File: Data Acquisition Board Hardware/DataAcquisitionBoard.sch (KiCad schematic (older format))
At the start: 10 parts, among them P1 BNC, P2 BNC, P3 BNC, P4 BNC

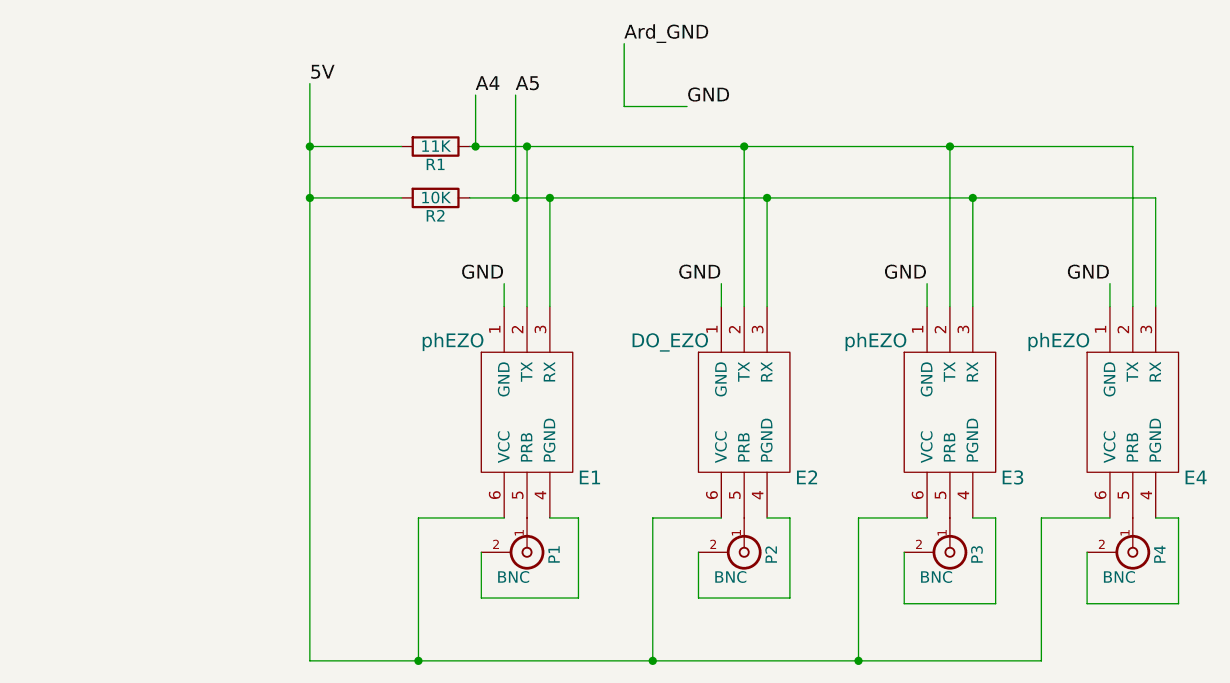
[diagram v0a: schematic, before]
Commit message: Completed PCB layout, added jumper footprint
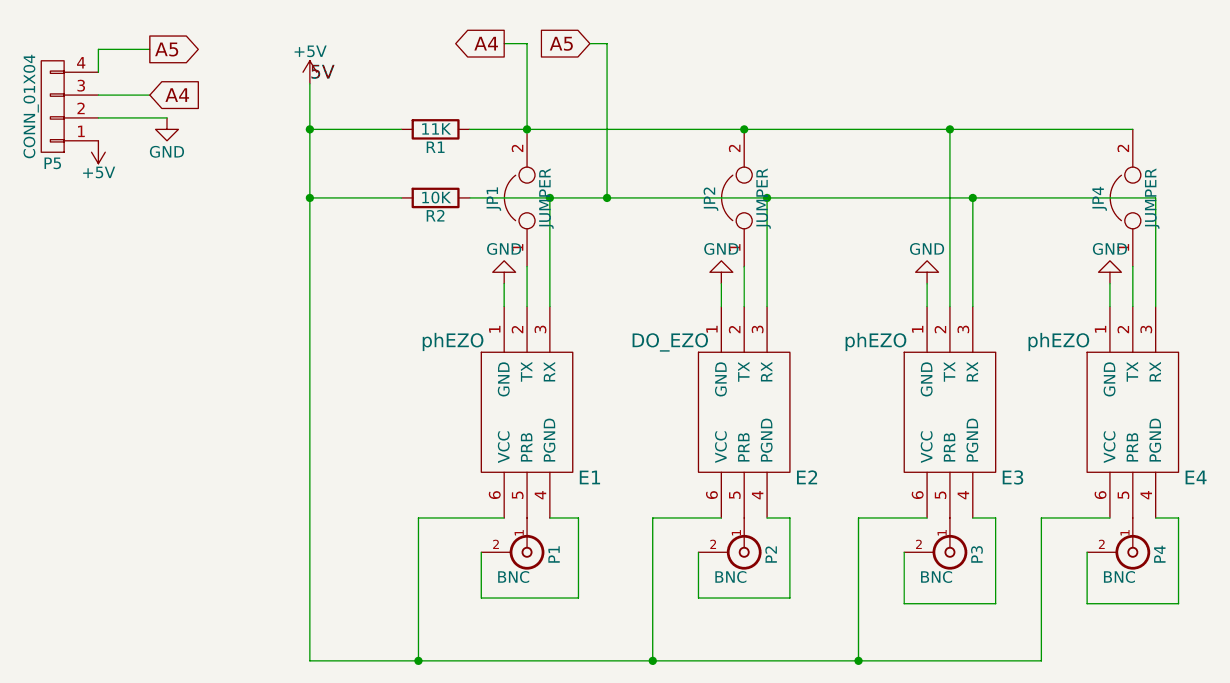
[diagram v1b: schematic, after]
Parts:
- added JP1, JP2, JP4: JUMPER, DAB:Jumper_6.35mm, symbol JUMPER
- added P5: CONN_01X04, Pin_Headers:Pin_Header_Straight_1x04, symbol CONN_01X04
- R1, R2: footprint Resistors_SMD:R_0805_HandSoldering -> Resistors_ThroughHole:Resistor_Horizontal_RM7mm
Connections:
- net A4: now also JP1.2, JP2.2, JP4.2, P5.3 (P3); no longer E1.2 (TX), E2.2 (TX), E4.2 (TX)
- net A5: now also P5.4 (P4)
- net 5V renamed +5V
- net +5V: now also P5.1 (P1)
- net Ard_GND renamed GND
- net GND: now also P5.2 (P2)
- new net: E1.2 (TX), JP1.1
- new net: E2.2 (TX), JP2.1
- new net: E4.2 (TX), JP4.1
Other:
- moved on the sheet: R1
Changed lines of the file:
@@
 	1    0    0    -1
 $EndComp
-Wire Wire Line
-	5375 3125 5500 3125
-Wire Wire Line
-	5500 3125 5500 3475
-Wire Wire Line
-	5500 3475 5075 3475
-Wire Wire Line
-	5075 3475 5075 3275
 $Comp
 L BNC P2
@@
 	0    1    1    0
 $EndComp
-Wire Wire Line
-	6325 3125 6425 3125
-Wire Wire Line
-	6425 3125 6425 3475
-Wire Wire Line
-	6425 3475 6025 3475
-Wire Wire Line
-	6025 3475 6025 3275
 Text Label 4325 1225 0    60   ~ 0
 5V
-Wire Wire Line
-	4325 1225 4325 3750
-Wire Wire Line
-	4325 3750 7525 3750
-Wire Wire Line
-	5825 3750 5825 3125
-Wire Wire Line
-	5825 3125 6125 3125
-Wire Wire Line
-	4800 3750 4800 3125
-Wire Wire Line
-	4800 3125 5175 3125
-Connection ~ 4800 3750
 $Comp
 L phEZO E3
@@
 	0    1    1    0
 $EndComp
-Wire Wire Line
-	6925 3275 6925 3500
-Wire Wire Line
-	6925 3500 7325 3500
-Wire Wire Line
-	7325 3500 7325 3125
-Wire Wire Line
-	7325 3125 7225 3125
-Wire Wire Line
-	7725 3275 7725 3500
-Wire Wire Line
-	7725 3500 8125 3500
-Wire Wire Line
-	8125 3500 8125 3125
-Wire Wire Line
-	8125 3125 8025 3125
-Wire Wire Line
-	6725 3750 6725 3125
-Wire Wire Line
-	6725 3125 7025 3125
-Connection ~ 5825 3750
-Wire Wire Line
-	7525 3750 7525 3125
-Wire Wire Line
-	7525 3125 7825 3125
-Connection ~ 6725 3750
-Wire Wire Line
-	7825 2200 7825 2100
-Text Label 7825 2100 2    60   ~ 0
-GND
-Text Label 5975 1325 0    60   ~ 0
-GND
-Wire Wire Line
-	7025 2200 7025 2100
-Text Label 7025 2100 2    60   ~ 0
-GND
-Wire Wire Line
-	6125 2200 6125 2100
-Text Label 6125 2100 2    60   ~ 0
-GND
-Wire Wire Line
-	5175 2200 5175 2100
-Text Label 5175 2100 2    60   ~ 0
-GND
-Text Label 5050 1275 0    60   ~ 0
-A4
 $Comp
 L R R1
 U 1 1 5848F097
-P 4875 1500
-F 0 "R1" V 4955 1500 50  0000 C CNN
-F 1 "11K" V 4875 1500 50  0000 C CNN
-F 2 "Resistors_SMD:R_0805_HandSoldering" V 4805 1500 50  0001 C CNN
-F 3 "" H 4875 1500 50  0000 C CNN
-	1    4875 1500
+P 4875 1425
+F 0 "R1" V 4955 1425 50  0000 C CNN
+F 1 "11K" V 4875 1425 50  0000 C CNN
+F 2 "Resistors_ThroughHole:Resistor_Horizontal_RM7mm" V 4805 1425 50  0001 C CNN
+F 3 "" H 4875 1425 50  0000 C CNN
+	1    4875 1425
 	0    1    1    0
 $EndComp
@@
 F 0 "R2" V 4955 1725 50  0000 C CNN
 F 1 "10K" V 4875 1725 50  0000 C CNN
-F 2 "Resistors_SMD:R_0805_HandSoldering" V 4805 1725 50  0001 C CNN
+F 2 "Resistors_ThroughHole:Resistor_Horizontal_RM7mm" V 4805 1725 50  0001 C CNN
 F 3 "" H 4875 1725 50  0000 C CNN
 	1    4875 1725
 	0    1    1    0
 $EndComp
-Wire Wire Line
-	4325 1500 4725 1500
-Connection ~ 4325 1500
-Wire Wire Line
-	5025 1500 7925 1500
-Wire Wire Line
-	5275 1500 5275 2200
+$Comp
+L CONN_01X04 P5
+U 1 1 5849CBF9
+P 3200 1325
+F 0 "P5" H 3200 1575 50  0000 C CNN
+F 1 "CONN_01X04" V 3300 1325 50  0000 C CNN
+F 2 "Pin_Headers:Pin_Header_Straight_1x04" H 3200 1325 50  0001 C CNN
+F 3 "" H 3200 1325 50  0000 C CNN
+	1    3200 1325
+	-1   0    0    1
+$EndComp
+$Comp
+L +5V #PWR01
+U 1 1 584C80B9
+P 4325 1225
+F 0 "#PWR01" H 4325 1075 50  0001 C CNN
+F 1 "+5V" H 4325 1365 50  0000 C CNN
+F 2 "" H 4325 1225 50  0000 C CNN
+F 3 "" H 4325 1225 50  0000 C CNN
+	1    4325 1225
+	1    0    0    -1
+$EndComp
+$Comp
+L JUMPER JP1
+U 1 1 584C8796
+P 5275 1725
+F 0 "JP1" H 5275 1875 50  0000 C CNN
+F 1 "JUMPER" H 5275 1645 50  0000 C CNN
+F 2 "DAB:Jumper_6.35mm" H 5275 1725 50  0001 C CNN
+F 3 "" H 5275 1725 50  0000 C CNN
+	1    5275 1725
+	0    -1   -1   0
+$EndComp
+$Comp
+L JUMPER JP2
+U 1 1 584C89B3
+P 6225 1725
+F 0 "JP2" H 6225 1875 50  0000 C CNN
+F 1 "JUMPER" H 6225 1645 50  0000 C CNN
+F 2 "DAB:Jumper_6.35mm" H 6225 1725 50  0001 C CNN
+F 3 "" H 6225 1725 50  0000 C CNN
+	1    6225 1725
+	0    -1   -1   0
+$EndComp
+$Comp
+L JUMPER JP4
+U 1 1 584C8A2C
+P 7925 1725
+F 0 "JP4" H 7925 1875 50  0000 C CNN
+F 1 "JUMPER" H 7925 1645 50  0000 C CNN
+F 2 "DAB:Jumper_6.35mm" H 7925 1725 50  0001 C CNN
+F 3 "" H 7925 1725 50  0000 C CNN
+	1    7925 1725
+	0    -1   -1   0
+$EndComp
+Wire Wire Line
+	5375 3125 5500 3125
+Wire Wire Line
+	5500 3125 5500 3475
+Wire Wire Line
+	5500 3475 5075 3475
+Wire Wire Line
+	5075 3475 5075 3275
+Wire Wire Line
+	6325 3125 6425 3125
+Wire Wire Line
+	6425 3125 6425 3475
+Wire Wire Line
+	6425 3475 6025 3475
+Wire Wire Line
+	6025 3475 6025 3275
+Wire Wire Line
+	4325 1225 4325 3750
+Wire Wire Line
+	4325 3750 7525 3750
+Wire Wire Line
+	5825 3750 5825 3125
+Wire Wire Line
+	5825 3125 6125 3125
+Wire Wire Line
+	4800 3750 4800 3125
+Wire Wire Line
+	4800 3125 5175 3125
+Connection ~ 4800 3750
+Wire Wire Line
+	6925 3275 6925 3500
+Wire Wire Line
+	6925 3500 7325 3500
+Wire Wire Line
+	7325 3500 7325 3125
+Wire Wire Line
+	7325 3125 7225 3125
+Wire Wire Line
+	7725 3275 7725 3500
+Wire Wire Line
+	7725 3500 8125 3500
+Wire Wire Line
+	8125 3500 8125 3125
+Wire Wire Line
+	8125 3125 8025 3125
+Wire Wire Line
+	6725 3750 6725 3125
+Wire Wire Line
+	6725 3125 7025 3125
+Connection ~ 5825 3750
+Wire Wire Line
+	7525 3750 7525 3125
+Wire Wire Line
+	7525 3125 7825 3125
+Connection ~ 6725 3750
+Wire Wire Line
+	7825 2200 7825 2100
+Wire Wire Line
+	7025 2200 7025 2100
+Wire Wire Line
+	6125 2200 6125 2100
+Wire Wire Line
+	5175 2200 5175 2100
+Wire Wire Line
+	4325 1425 4725 1425
+Connection ~ 4325 1425
+Wire Wire Line
+	5025 1425 7925 1425
 Wire Wire Line
 	4325 1725 4725 1725
 Connection ~ 4325 1725
-Text Label 5225 1275 0    60   ~ 0
-A5
-Wire Wire Line
-	7925 1500 7925 2200
-Connection ~ 5275 1500
-Wire Wire Line
-	7125 2200 7125 1500
-Connection ~ 7125 1500
-Wire Wire Line
-	6225 2200 6225 1500
-Connection ~ 6225 1500
-Wire Wire Line
-	5050 1275 5050 1500
-Connection ~ 5050 1500
-Wire Wire Line
-	5225 1275 5225 1725
+Connection ~ 5275 1425
+Connection ~ 7125 1425
+Connection ~ 6225 1425
 Wire Wire Line
 	5025 1725 8025 1725
 Wire Wire Line
 	8025 1725 8025 2200
-Connection ~ 5225 1725
 Wire Wire Line
 	5375 2200 5375 1725
@@
 	7225 2200 7225 1725
 Connection ~ 7225 1725
-Text Label 5700 1050 0    60   ~ 0
-Ard_GND
-Wire Wire Line
-	5700 1325 5700 1050
-Wire Wire Line
-	5700 1325 5975 1325
+Wire Wire Line
+	5275 2200 5275 2025
+Wire Wire Line
+	6225 2200 6225 2025
+Wire Wire Line
+	7125 1425 7125 2200
+Wire Wire Line
+	7925 2200 7925 2025
+Text GLabel 3625 1275 2    60   Input ~ 0
+A4
+Text GLabel 5550 1050 0    60   Input ~ 0
+A5
+Text GLabel 5175 1050 0    60   Output ~ 0
+A4
+Text GLabel 3625 1075 2    60   Output ~ 0
+A5
+Wire Wire Line
+	3400 1275 3625 1275
+Wire Wire Line
+	3400 1175 3400 1075
+Wire Wire Line
+	3400 1075 3625 1075
+$Comp
+L GND #PWR02
+U 1 1 584C9542
+P 3700 1375
+F 0 "#PWR02" H 3700 1125 50  0001 C CNN
+F 1 "GND" H 3700 1225 50  0000 C CNN
+F 2 "" H 3700 1375 50  0000 C CNN
+F 3 "" H 3700 1375 50  0000 C CNN
+	1    3700 1375
+	1    0    0    -1
+$EndComp
+Wire Wire Line
+	3400 1375 3700 1375
+$Comp
+L +5V #PWR03
+U 1 1 584C962E
+P 3400 1475
+F 0 "#PWR03" H 3400 1325 50  0001 C CNN
+F 1 "+5V" H 3400 1615 50  0000 C CNN
+F 2 "" H 3400 1475 50  0000 C CNN
+F 3 "" H 3400 1475 50  0000 C CNN
+	1    3400 1475
+	-1   0    0    1
+$EndComp
+Wire Wire Line
+	5275 1425 5275 1050
+Wire Wire Line
+	5275 1050 5175 1050
+Wire Wire Line
+	5625 1050 5625 1725
+Connection ~ 5625 1725
+Wire Wire Line
+	5550 1050 5625 1050
+$Comp
+L GND #PWR04
+U 1 1 584C9BAF
+P 5175 2100
+F 0 "#PWR04" H 5175 1850 50  0001 C CNN
+F 1 "GND" H 5175 1950 50  0000 C CNN
+F 2 "" H 5175 2100 50  0000 C CNN
+F 3 "" H 5175 2100 50  0000 C CNN
+	1    5175 2100
+	-1   0    0    1
+$EndComp
+$Comp
+L GND #PWR05
+U 1 1 584C9C26
+P 6125 2100
+F 0 "#PWR05" H 6125 1850 50  0001 C CNN
+F 1 "GND" H 6125 1950 50  0000 C CNN
+F 2 "" H 6125 2100 50  0000 C CNN
+F 3 "" H 6125 2100 50  0000 C CNN
+	1    6125 2100
+	-1   0    0    1
+$EndComp
+$Comp
+L GND #PWR06
+U 1 1 584C9C5E
+P 7025 2100
+F 0 "#PWR06" H 7025 1850 50  0001 C CNN
+F 1 "GND" H 7025 1950 50  0000 C CNN
+F 2 "" H 7025 2100 50  0000 C CNN
+F 3 "" H 7025 2100 50  0000 C CNN
+	1    7025 2100
+	-1   0    0    1
+$EndComp
+$Comp
+L GND #PWR07
+U 1 1 584C9C96
+P 7825 2100
+F 0 "#PWR07" H 7825 1850 50  0001 C CNN
+F 1 "GND" H 7825 1950 50  0000 C CNN
+F 2 "" H 7825 2100 50  0000 C CNN
+F 3 "" H 7825 2100 50  0000 C CNN
+	1    7825 2100
+	-1   0    0    1
+$EndComp
 $EndSCHEMATC
